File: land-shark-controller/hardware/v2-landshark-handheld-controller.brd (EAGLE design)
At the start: 93.2 x 50.8 mm, 7 parts

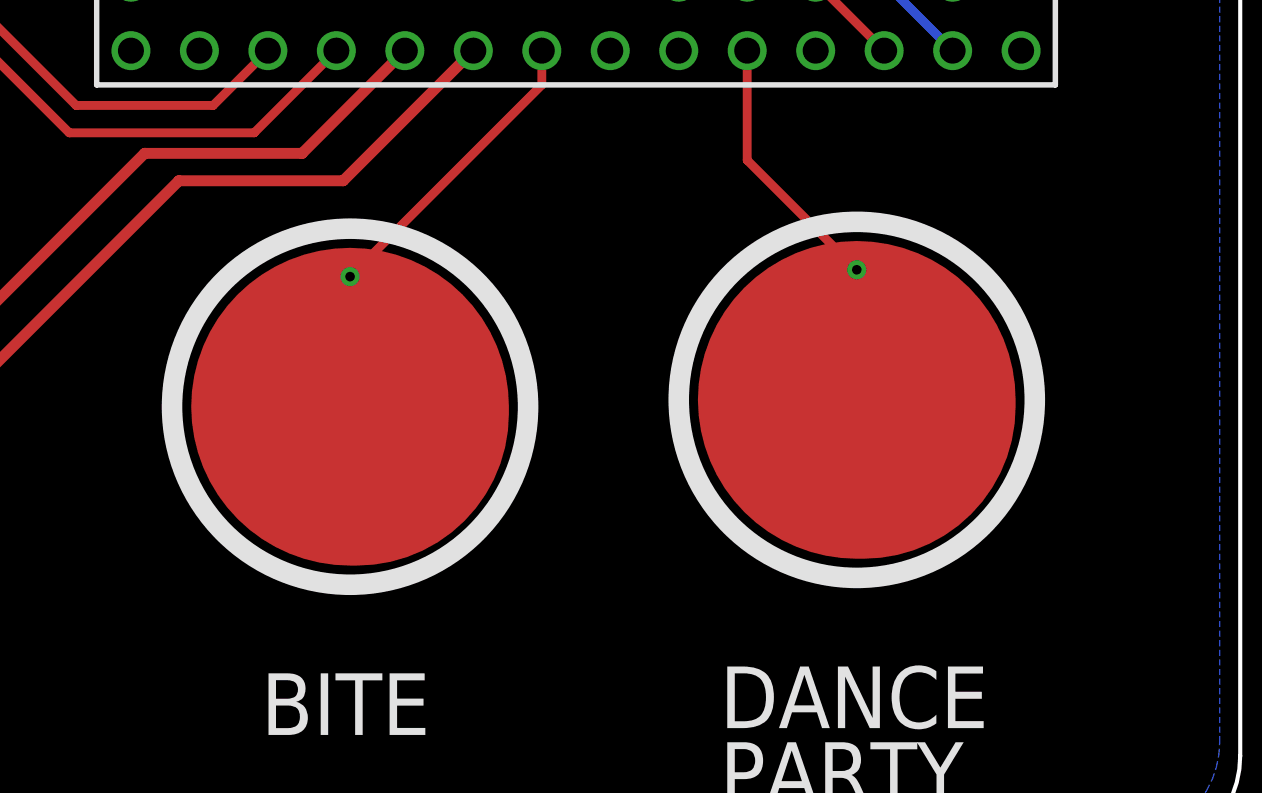
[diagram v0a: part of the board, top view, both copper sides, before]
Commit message: Added shark images to BITE and DANCE PARTY. Board file ready for gerberizing.
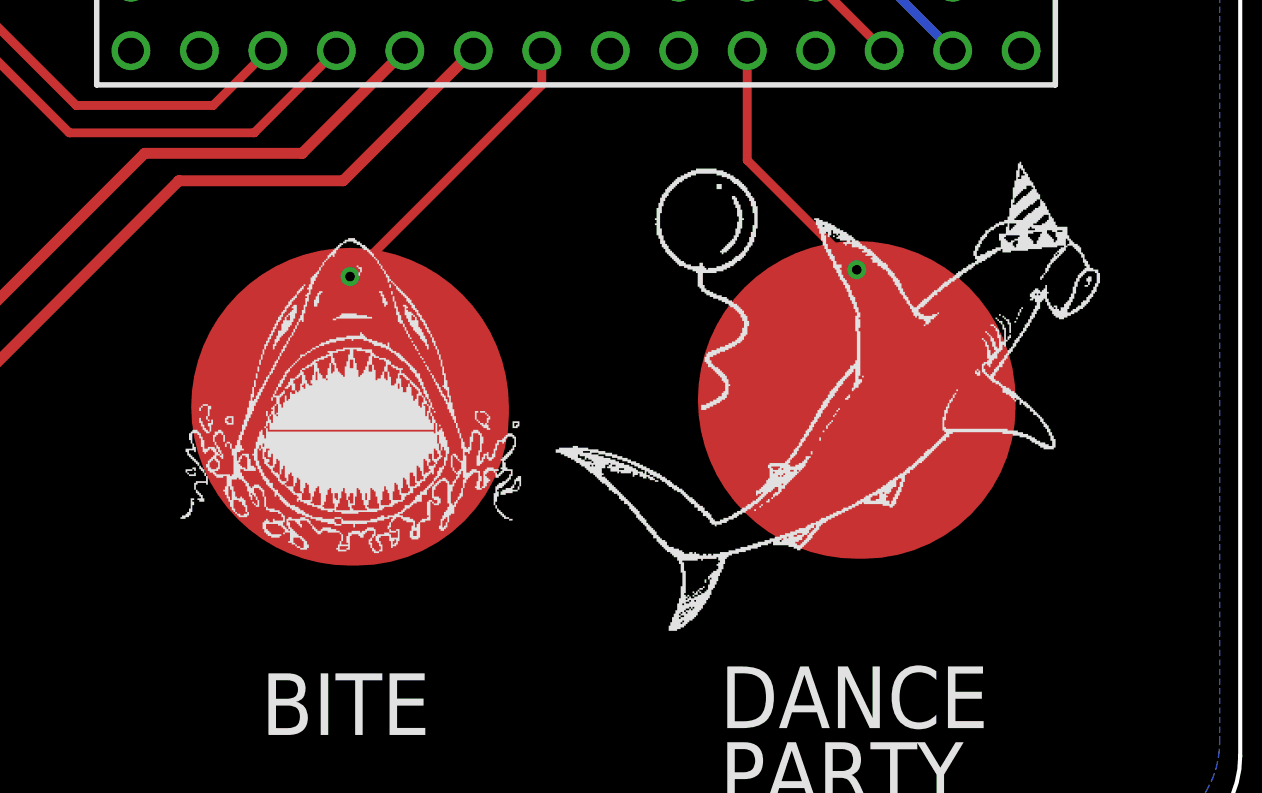
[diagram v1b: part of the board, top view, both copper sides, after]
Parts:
- BITE: device PatternAgents-TouchWidgets:BUTTON_PASSIVE_12MM -> PatternAgents-TouchWidgets:BUTTON_PASSIVE_12MM_BITE
- DANCE: device PatternAgents-TouchWidgets:BUTTON_PASSIVE_12MM -> PatternAgents-TouchWidgets:BUTTON_PASSIVE_12MM_DANCE
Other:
- board text added: "v2 Proto 25-Aug-2015 OSH PARK Many thanks to Pattern Agents!"
- board text removed: "v1 Proto 19-Aug-2015"

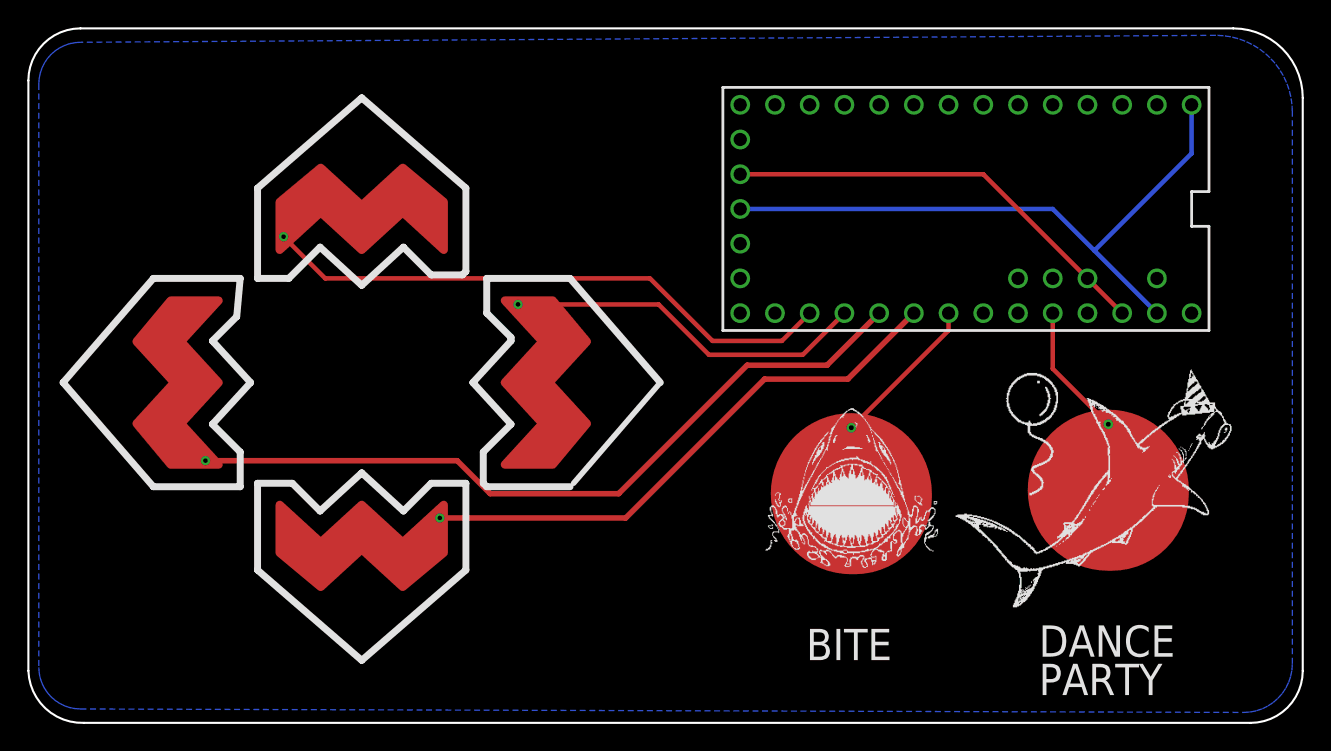
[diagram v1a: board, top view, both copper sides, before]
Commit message: Moved traces to bottom layer. Added top ground plane with 40 mils isolation.
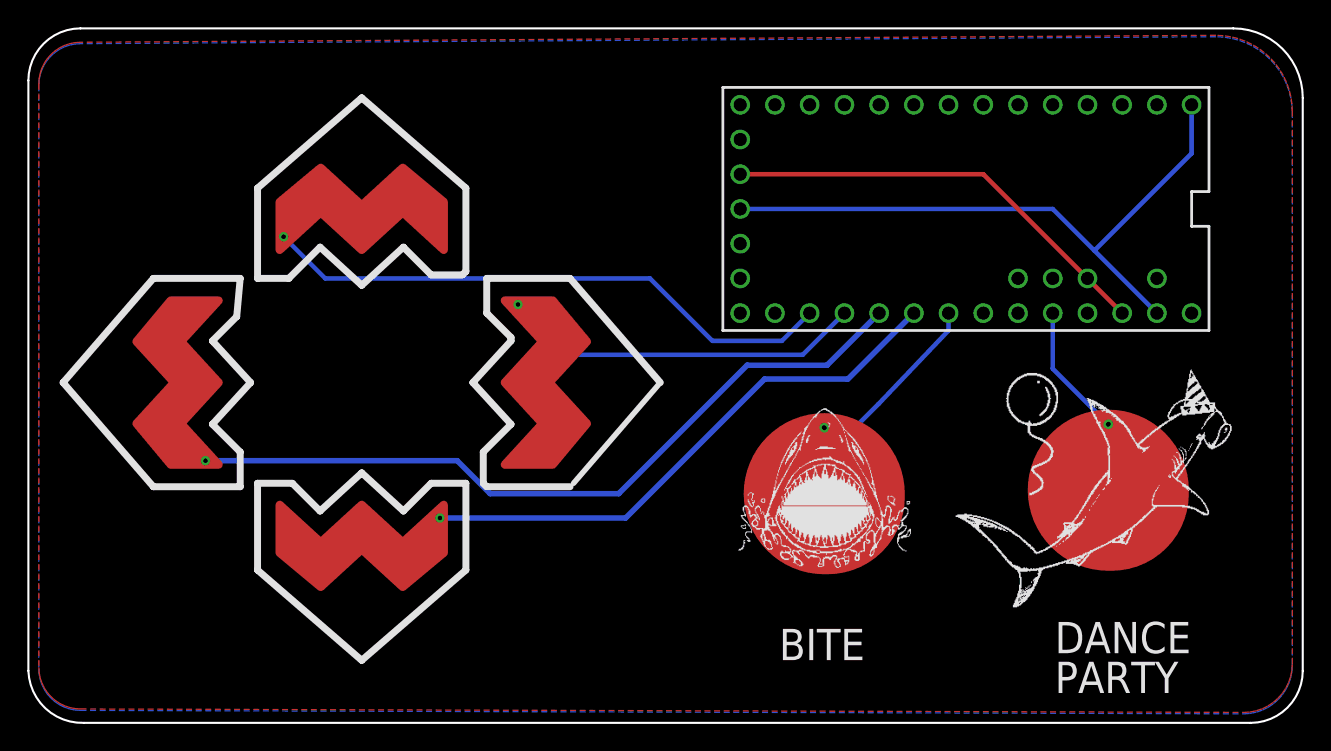
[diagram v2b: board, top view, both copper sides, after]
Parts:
- moved BITE 1.98 mm to (58.2, 16.8)
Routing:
- net BITE: track 11.3 -> 13.4 mm
- added copper zone on layer 1, net GND
